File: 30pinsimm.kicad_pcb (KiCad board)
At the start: 4 copper layers, 89 x 16.6 mm, 7 parts, among them U1 JEDEC-FPDRAM_xMbx4, U2 JEDEC-FPDRAM_xMbx4, U3 JEDEC-FPDRAM_xMbx1

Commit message: alingment
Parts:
- moved U1 0.13 mm to (119.5, 100.8)
- moved U3 0.13 mm to (168.8, 100.7)

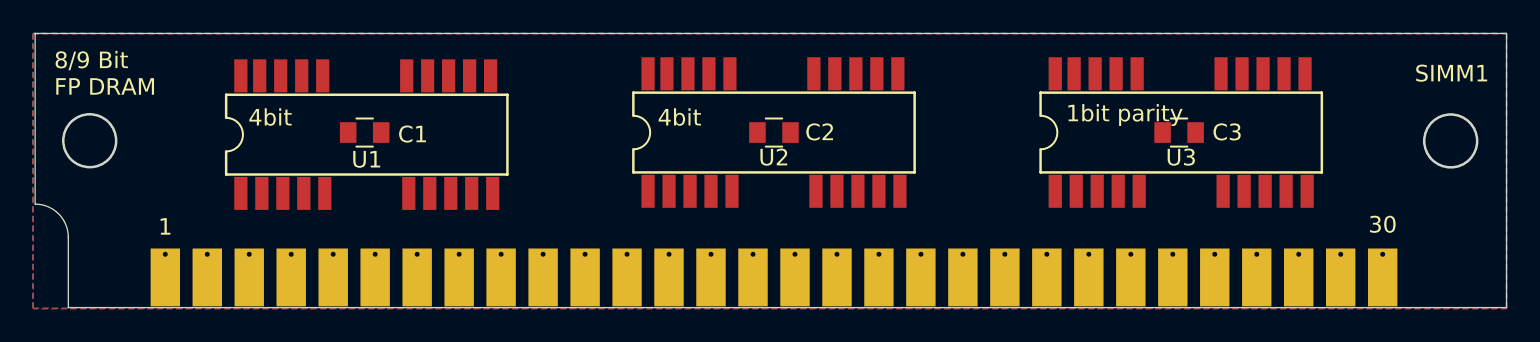
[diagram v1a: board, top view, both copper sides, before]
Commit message: updated the 4Mb module
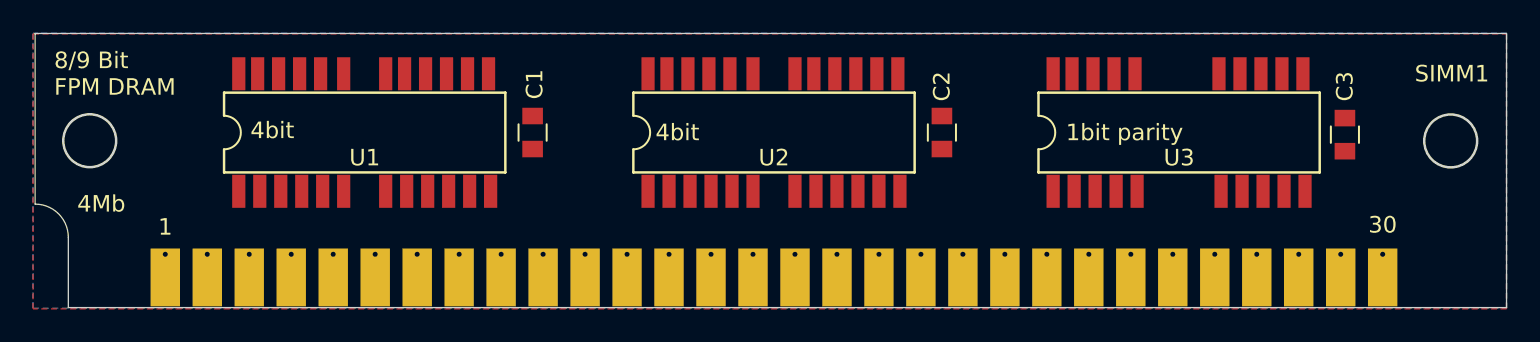
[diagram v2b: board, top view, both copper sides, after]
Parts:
- U1, U2: value JEDEC-FPDRAM_xMbx4 -> 4Mx4FPMDRAM; footprint Sebs:SOJ-20-26-2 -> Sebs:SOJ-24
- U3: value JEDEC-FPDRAM_xMbx1 -> 4Mx1FPMDRAM; footprint Sebs:SOJ-20-26-2 -> Sebs:SOJ-20
- moved C1 10.2 mm to (129.5, 100.7), turned to 270 degrees
- moved C2 10.2 mm to (154.3, 100.7), turned to 270 degrees
- moved C3 10.0 mm to (178.7, 100.8), turned to 270 degrees
- moved U1 0.18 mm to (119.4, 100.7)
- moved U3 0.13 mm to (168.7, 100.7)
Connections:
- U1 pad 1: /DQ0 -> +5V
- U1 pad 10: +5V -> /A1
- U1 pad 11: /A4 -> /A2
- U1 pad 12: /A5 -> /A3
- U1 pad 13: /A6 -> +5V
- U1 pad 14: /A7 -> GND
- U1 pad 15: /A8 -> /A4
- U1 pad 16: GND -> /A5
- U1 pad 17: /CAS -> /A6
- U1 pad 18: /DQ2 -> /A7
- U1 pad 19: /DQ3 -> /A8
- U1 pad 2: /DQ1 -> /DQ0
- U1 pad 3: /WE -> /DQ1
- U1 pad 4: /RAS -> /WE
- U1 pad 5: /A9 -> /RAS
- U1 pad 6: /A1 -> Net-(U1-Pad6)
- U1 pad 8: /A2 -> /A10
- U1 pad 9: /A3 -> /A1
- U2 pad 1: /DQ4 -> +5V
- U2 pad 10: +5V -> /A1
- U2 pad 11: /A4 -> /A2
- U2 pad 12: /A5 -> /A3
- U2 pad 13: /A6 -> +5V
- U2 pad 14: /A7 -> GND
- U2 pad 15: /A8 -> /A4
- U2 pad 16: GND -> /A5
- U2 pad 17: /CAS -> /A6
- U2 pad 18: /DQ6 -> /A7
- U2 pad 19: /DQ7 -> /A8
- U2 pad 2: /DQ5 -> /DQ4
- U2 pad 3: /WE -> /DQ5
- U2 pad 4: /RAS -> /WE
- U2 pad 5: /A9 -> /RAS
- U2 pad 6: /A0 -> Net-(U2-Pad6)
- U2 pad 8: /A2 -> Net-(U2-Pad8)
- U2 pad 9: /A3 -> /A0
- U3 pad 10: +5V -> /A1
- U3 pad 11: /A4 -> /A2
- U3 pad 12: /A5 -> /A3
- U3 pad 13: /A6 -> +5V
- U3 pad 14: /A7 -> /A4
- U3 pad 15: /A8 -> /A5
- U3 pad 16: /A9 -> /A6
- U3 pad 17: Net-(U3-Pad17) -> /A7
- U3 pad 18: /CASP -> /A8
- U3 pad 5: Net-(U3-Pad5) -> /A10
- U3 pad 9: /A3 -> /A0
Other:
- board text added: "4Mb"
- board text added: "8/9 Bit FPM DRAM"
- board text removed: "8/9 Bit FP DRAM"

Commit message: general updates
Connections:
- U1 pad 22: Net-(U1-Pad22) -> GND
- U2 pad 22: Net-(U2-Pad22) -> GND
- U2 pad 8: Net-(U2-Pad8) -> /A10
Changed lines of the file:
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@@
     (zones 0)
     (modules 7)
-    (nets 36)
+    (nets 33)
   )
   (page A4)
@@
   (net 29 "Net-(U3-Pad4)")
   (net 30 "Net-(U1-Pad6)")
-  (net 31 "Net-(U1-Pad22)")
-  (net 32 "Net-(U2-Pad8)")
-  (net 33 "Net-(U2-Pad6)")
-  (net 34 "Net-(U2-Pad22)")
-  (net 35 "Net-(U3-Pad23)")
+  (net 31 "Net-(U2-Pad6)")
+  (net 32 "Net-(U3-Pad23)")
   (net_class Default "This is the default net class."
     (clearance 0.2)
@@
     (add_net /WE)
     (add_net GND)
-    (add_net "Net-(U1-Pad22)")
     (add_net "Net-(U1-Pad6)")
-    (add_net "Net-(U2-Pad22)")
     (add_net "Net-(U2-Pad6)")
-    (add_net "Net-(U2-Pad8)")
     (add_net "Net-(U3-Pad23)")
     (add_net "Net-(U3-Pad4)")
@@
       (net 12 /A9))
     (pad 23 smd rect (at -3.937 -3.556) (size 0.8 2) (layers F.Cu F.Paste F.Mask)
-      (net 35 "Net-(U3-Pad23)"))
+      (net 32 "Net-(U3-Pad23)"))
     (pad 24 smd rect (at -5.207 -3.556) (size 0.8 2) (layers F.Cu F.Paste F.Mask)
       (net 5 /CASP))
@@
       (net 12 /A9))
     (pad 8 smd rect (at 1.27 3.556) (size 0.8 2) (layers F.Cu F.Paste F.Mask)
-      (net 32 "Net-(U2-Pad8)"))
+      (net 7 /A10))
     (pad 6 smd rect (at -1.27 3.556) (size 0.8 2) (layers F.Cu F.Paste F.Mask)
-      (net 33 "Net-(U2-Pad6)"))
+      (net 31 "Net-(U2-Pad6)"))
     (pad 14 smd rect (at 7.493 -3.556) (size 0.8 2) (layers F.Cu F.Paste F.Mask)
       (net 11 GND))
@@
       (net 20 /A7))
     (pad 22 smd rect (at -2.667 -3.556) (size 0.8 2) (layers F.Cu F.Paste F.Mask)
-      (net 34 "Net-(U2-Pad22)"))
+      (net 11 GND))
     (pad 23 smd rect (at -3.937 -3.556) (size 0.8 2) (layers F.Cu F.Paste F.Mask)
       (net 28 /CAS))
@@
       (net 20 /A7))
     (pad 22 smd rect (at -2.667 -3.556) (size 0.8 2) (layers F.Cu F.Paste F.Mask)
-      (net 31 "Net-(U1-Pad22)"))
+      (net 11 GND))
     (pad 23 smd rect (at -3.937 -3.556) (size 0.8 2) (layers F.Cu F.Paste F.Mask)
       (net 28 /CAS))

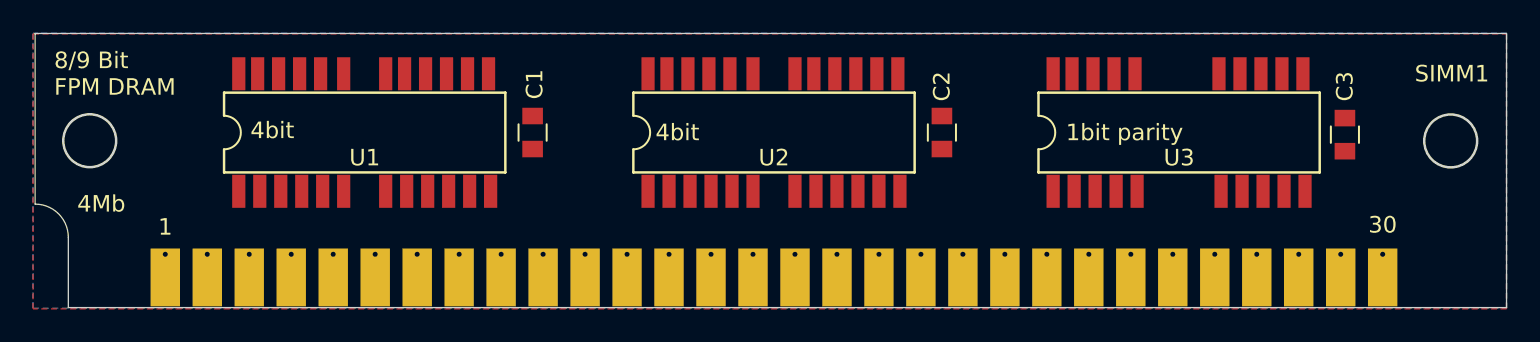
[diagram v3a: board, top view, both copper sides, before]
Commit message: 2sig 2 pwr layer routing
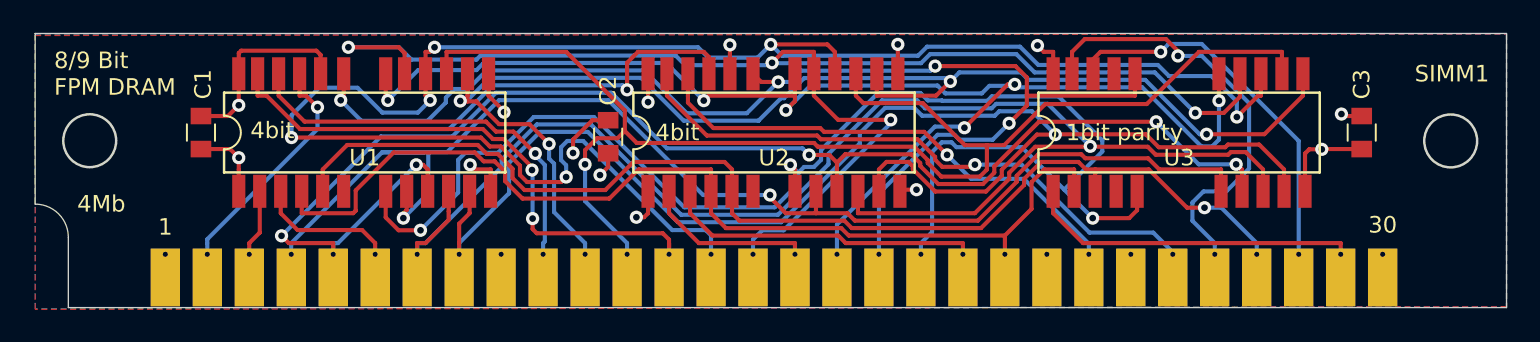
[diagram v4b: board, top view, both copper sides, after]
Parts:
- moved C2 20.2 mm to (134.1, 101.0)
- moved C1 20.1 mm to (109.5, 100.7)
- moved C3 1.02 mm to (179.7, 100.7)
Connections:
- U1 pad 9: /A1 -> /A0
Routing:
- net /A6: track 0.00 -> 108.6 mm, vias 0 -> 6
- net /A2: track 0.00 -> 86.2 mm, vias 0 -> 1
- net /A7: track 0.00 -> 86.0 mm, vias 0 -> 4
- net /A10: track 0.00 -> 85.2 mm, vias 0 -> 3
- net /A1: track 0.00 -> 84.3 mm, vias 0 -> 5
- net /A3: track 0.00 -> 81.9 mm, vias 0 -> 1
- net /A5: track 0.00 -> 81.9 mm, vias 0 -> 1
- net /A8: track 0.00 -> 79.8 mm, vias 0 -> 6
- net /A4: track 0.00 -> 79.7 mm, vias 0 -> 4
- net /A0: track 0.00 -> 77.5 mm, vias 0 -> 2
- net /A9: track 0.00 -> 74.1 mm, vias 0 -> 4
- net /RAS: track 0.00 -> 69.7 mm, vias 0 -> 1
- net /WE: track 0.00 -> 60.8 mm
- net /CAS: track 0.00 -> 42.3 mm, vias 0 -> 2
- net /DQ7: track 0.00 -> 36.2 mm, vias 0 -> 1
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- added copper zone on B.Cu, net (none)
- added copper zone on F.Cu, net (none)
- added copper zone on In1.Cu, net +5V
- added copper zone on In2.Cu, net GND
- removed copper zone on F.Cu, net +5V
- removed copper zone on B.Cu, net GND

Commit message: updates
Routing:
- net /A8: track 79.8 -> 83.3 mm
- net /A9: track 74.1 -> 75.9 mm
- net /A7: track 86.0 -> 87.6 mm
- net /CAS: track 42.3 -> 43.0 mm
- net /A0: track 77.5 -> 78.1 mm
- net /A1: track 84.3 -> 84.9 mm
- net GND: track 27.1 -> 27.7 mm
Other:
- board text added: "https://pcb.hegars.com/?sku=4mbfpmsimm?sn="
- board text removed: "1bit parity"
- board text removed: "4bit"
- board text removed: "https://pcb.hegars.com/?sku=30pSIMM?size="

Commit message: updates
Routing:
- net /A1: track 84.9 -> 89.4 mm
- net /A7: track 87.6 -> 89.9 mm
- net /A9: track 75.9 -> 73.9 mm
- net /A10: track 85.2 -> 86.7 mm
- net /A5: track 81.5 -> 82.3 mm
- net /A0: track 78.1 -> 77.5 mm
